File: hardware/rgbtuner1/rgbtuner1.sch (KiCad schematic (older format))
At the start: 2 parts

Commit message: some components
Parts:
- added U?: LPC811, symbol LPC811
- added U?: AL3158, symbol AL3158
- added X?: 25 MHz, symbol CRYSTAL
- D?: Description (none) -> LED 5MM RGB 640/515/461NM CLR TH; Manufacturer (none) -> Kingbright; Part Number (none) -> WP154A4SUREQBFZGC
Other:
- note added: "B G R"
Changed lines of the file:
@@
 LIBS:valves
 LIBS:rgbtuner
+LIBS:rgbtuner1-cache
 EELAYER 27 0
 EELAYER END
@@
 F 2 "~" H 4600 4100 60  0000 C CNN
 F 3 "~" H 4600 4100 60  0000 C CNN
+F 4 "Kingbright" H 4600 4100 60  0001 C CNN "Manufacturer"
+F 5 "WP154A4SUREQBFZGC" H 4600 4100 60  0001 C CNN "Part Number"
+F 6 "LED 5MM RGB 640/515/461NM CLR TH" H 4600 4100 60  0001 C CNN "Description"
 	1    4600 4100
 	0    1    1    0
@@
 Wire Wire Line
 	4450 4400 4450 4500
+$Comp
+L LPC811 U?
+U 1 1 530555B6
+P 5600 2650
+F 0 "U?" V 5550 2650 60  0000 C CNN
+F 1 "LPC811" V 5650 2650 60  0000 C CNN
+F 2 "" H 5600 2650 60  0000 C CNN
+F 3 "" H 5600 2650 60  0000 C CNN
+F 4 "NXP" H 5600 2650 60  0001 C CNN "Manufacturer"
+F 5 "LPC811M001JDH16FP" H 5600 2650 60  0001 C CNN "Part Number"
+F 6 "IC MCU ARM 8KB FLASH 16TSSOP" H 5600 2650 60  0001 C CNN "Description"
+	1    5600 2650
+	1    0    0    -1
+$EndComp
+Text Notes 4250 3800 0    60   ~ 0
+B  G  R
+$Comp
+L AL3158 U?
+U 1 1 53055893
+P 3350 2500
+F 0 "U?" H 3350 2550 60  0000 C CNN
+F 1 "AL3158" H 3350 2450 60  0000 C CNN
+F 2 "" H 3350 2500 60  0000 C CNN
+F 3 "" H 3350 2500 60  0000 C CNN
+F 4 "Diodes Inc." H 3350 2500 60  0001 C CNN "Manufacturer"
+F 5 "AL3158FSG-7" H 3350 2500 60  0001 C CNN "Part Number"
+F 6 "IC LED DRVR CHG/PMP QFN3030-20" H 3350 2500 60  0001 C CNN "Description"
+	1    3350 2500
+	1    0    0    -1
+$EndComp
+$Comp
+L CRYSTAL X?
+U 1 1 53055B71
+P 5550 1700
+F 0 "X?" H 5550 1850 60  0000 C CNN
+F 1 "25 MHz" H 5550 1550 60  0000 C CNN
+F 2 "" H 5550 1700 60  0000 C CNN
+F 3 "" H 5550 1700 60  0000 C CNN
+F 4 "Abracon" H 5550 1700 60  0001 C CNN "Manufacturer"
+F 5 "ABLS-25.000MHZ-B4-F-T" H 5550 1700 60  0001 C CNN "Part Number"
+F 6 "CRYSTAL 25MHZ 18PF SMD" H 5550 1700 60  0001 C CNN "Description"
+	1    5550 1700
+	1    0    0    -1
+$EndComp
 $EndSCHEMATC

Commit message: switched to common-anode RGB LED
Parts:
- D?: value LED-RGB-WP154 -> RGB; symbol LED-RGB-WP154 -> LED-RGB-COMMON-ANODE; Description LED 5MM RGB 640/515/461NM CLR TH -> LED - RGB Clear Common Anode; Manufacturer Kingbright -> China Young Sun LED; Note (none) -> Sparkfun COM-10820; Part Number WP154A4SUREQBFZGC -> YSL-R596AR3G4B5C-C10
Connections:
- wire segments 2 -> 1
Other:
- note removed: "B G R"
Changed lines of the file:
@@
 	1950 4350 1950 4450
 $Comp
-L LED-RGB-WP154 D?
+L LED-RGB-COMMON-ANODE D?
 U 1 1 53055340
 P 4600 4100
 F 0 "D?" H 4600 4200 50  0000 C CNN
-F 1 "LED-RGB-WP154" H 4600 3650 50  0000 C CNN
+F 1 "RGB" H 4600 3650 50  0000 C CNN
 F 2 "~" H 4600 4100 60  0000 C CNN
 F 3 "~" H 4600 4100 60  0000 C CNN
-F 4 "Kingbright" H 4600 4100 60  0001 C CNN "Manufacturer"
-F 5 "WP154A4SUREQBFZGC" H 4600 4100 60  0001 C CNN "Part Number"
-F 6 "LED 5MM RGB 640/515/461NM CLR TH" H 4600 4100 60  0001 C CNN "Description"
+F 4 "China Young Sun LED" H 4600 4100 60  0001 C CNN "Manufacturer"
+F 5 "YSL-R596AR3G4B5C-C10" H 4600 4100 60  0001 C CNN "Part Number"
+F 6 "LED - RGB Clear Common Anode" H 4600 4100 60  0001 C CNN "Description"
+F 7 "Sparkfun COM-10820" H 4600 4100 60  0001 C CNN "Note"
 	1    4600 4100
 	0    1    1    0
 $EndComp
-$Comp
-L GND #PWR?
-U 1 1 5305534F
-P 4450 4500
-F 0 "#PWR?" H 4450 4500 30  0001 C CNN
-F 1 "GND" H 4450 4430 30  0001 C CNN
-F 2 "" H 4450 4500 60  0000 C CNN
-F 3 "" H 4450 4500 60  0000 C CNN
-	1    4450 4500
-	1    0    0    -1
-$EndComp
-Wire Wire Line
-	4450 4400 4450 4500
 $Comp
 L LPC811 U?
@@
 	1    0    0    -1
 $EndComp
-Text Notes 4250 3800 0    60   ~ 0
-B  G  R
 $Comp
 L AL3158 U?

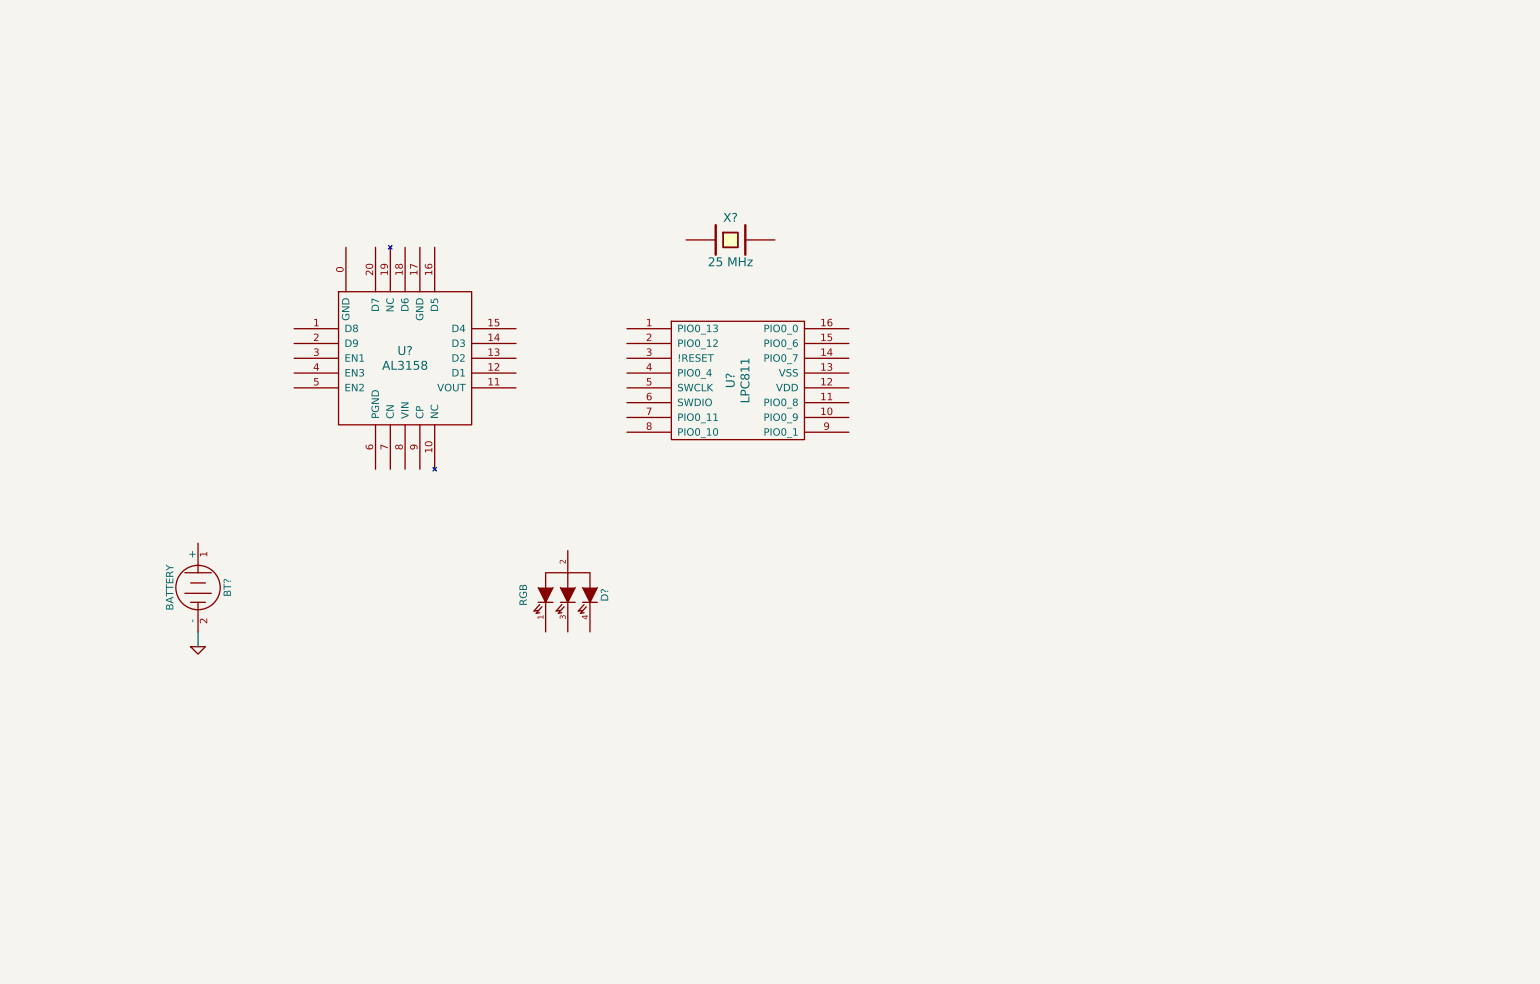
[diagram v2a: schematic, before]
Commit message: LED driver connections
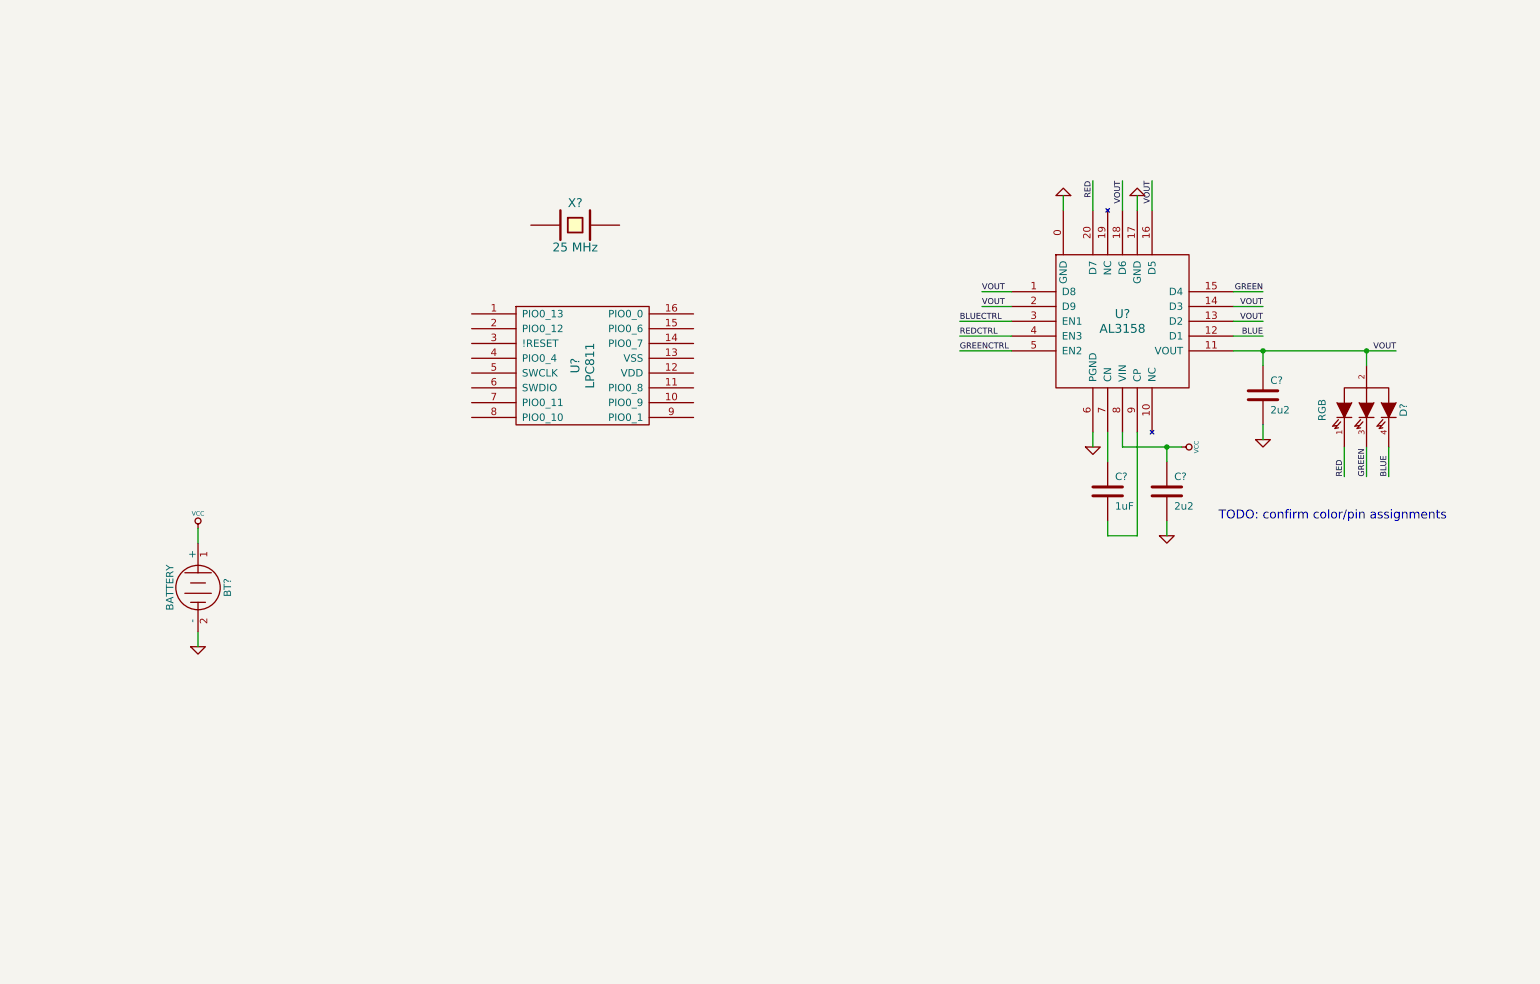
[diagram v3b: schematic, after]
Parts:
- added C? (x2): 2u2, symbol C
- added C?: 1uF, symbol C
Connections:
- net GND: now also U?.0 (GND), U?.17 (GND), U?.6 (PGND), C?.2, C?.2
- net VCC: now reaches BT?.1 (+)
- net VCC: now also U?.8 (VIN), C?.1
- net RED: now reaches D?.1 (RED)
- net RED: now also U?.20 (D7)
- net VOUT: now reaches D?.2 (A)
- net VOUT: now also U?.1 (D8), U?.11 (VOUT), U?.13 (D2), U?.14 (D3), U?.16 (D5), U?.18 (D6), U?.2 (D9), C?.1
- net GREEN: now reaches D?.3 (GREEN)
- net GREEN: now also U?.15 (D4)
- net BLUE: now reaches D?.4 (BLUE)
- net BLUE: now also U?.12 (D1)
- net BLUECTRL: now reaches U?.3 (EN1)
- net REDCTRL: now reaches U?.4 (EN3)
- net GREENCTRL: now reaches U?.5 (EN2)
- net at U?.7 (CN): now also C?.1
- net at U?.9 (CP): now also C?.2
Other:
- note added: "TODO: confirm color/pin assignments"
- moved on the sheet: D?, U?, X?

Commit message: MCU
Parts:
- added C? (x3): C, symbol C
- added P?: CONN_2, symbol CONN_2
- added R? (x7): 10k, symbol R
- U?: symbol LPC811 -> LPC812-20
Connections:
- net BLUECTRL: now also U?.2 (PIO0_13), R?.2
- net GND: now also U?.15 (VDD), C?.2, C?.2, C?.2, R?.1, R?.1, R?.1
- net GREENCTRL: now also U?.20 (PIO0_14), R?.2
- net REDCTRL: now also U?.1 (PIO0_17), R?.2
- net VCC: now also U?.16 (VSS), C?.1, P?.2 (PM), R?.1, R?.2, R?.2, R?.2; no longer BT?.1 (+)
- net S5: now reaches U?.10 (PIO0_16)
- net S2: now reaches U?.11 (PIO0_15)
- net LED1: now reaches U?.12 (PIO0_1)
- net LED1: now also R?.2
- net at U?.13 (PIO0_9): now also X?.2, C?.1
- net at U?.14 (PIO0_8): now also X?.1, C?.1
- net COMA: now reaches U?.3 (PIO0_12)
- net COMA: now also R?.1
- net RESET: now reaches U?.4 (!RESET)
- net RESET: now also R?.1
- net COMB: now reaches U?.5 (PIO0_4)
- net COMB: now also R?.1
- net SWCLK: now reaches U?.6 (SWCLK)
- net SWDIO: now reaches U?.7 (SWDIO)
- net S3: now reaches U?.8 (PIO0_11)
- net S4: now reaches U?.9 (PIO0_10)
- new net: BT?.1 (+), P?.1 (P1)
- new net LED2: U?.19 (PIO0_0)
- new net LED3: U?.18 (PIO0_6)
- new net LED4: U?.17 (PIO0_7)
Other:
- note added: "FIXME: WAKEUP"
- note added: "PCB jumper"
- note added: "TODO:\nSWD\nISP?\ndirectional input\ncharlieplexed indicator LEDs"
- moved on the sheet: X?

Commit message: charlieplexed indicator LEDs, WAKEUP fix
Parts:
- added D? (x10): LED, symbol LED
- added R? (x4): 10k, symbol R
- added R? (x4): R, symbol R
- C? (x2): value C -> 33pF
- R? (x2): value 10k -> 100k
- R?: Note (none) -> DNP
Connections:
- net COMA: now also R?.1, U?.5 (PIO0_4); no longer R?.1, U?.3 (PIO0_12)
- net COMB: now also R?.1, U?.3 (PIO0_12); no longer R?.1, U?.5 (PIO0_4)
- net GND: now also R?.1, R?.1, R?.1, R?.1
- net LED1: now also R?.1
- net LED2: now also R?.1
- net LED3: now also R?.1
- net LED4: now also R?.1
- net S2: now also R?.2
- net S3: now also R?.2
- net S4: now also R?.2
- net S5: now also R?.2
- new net: D?.1 (A), D?.1 (A), D?.2 (K), D?.2 (K), R?.2 (x2)
- new net: D?.1 (A), D?.1 (A), D?.1 (A), D?.2 (K), D?.2 (K), D?.2 (K), R?.2 (x2)
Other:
- note added: "TODO:\nSWD\nISP?\ndirectional input"
- note removed: "FIXME: WAKEUP"
- note removed: "TODO:\nSWD\nISP?\ndirectional input\ncharlieplexed indicator LEDs"

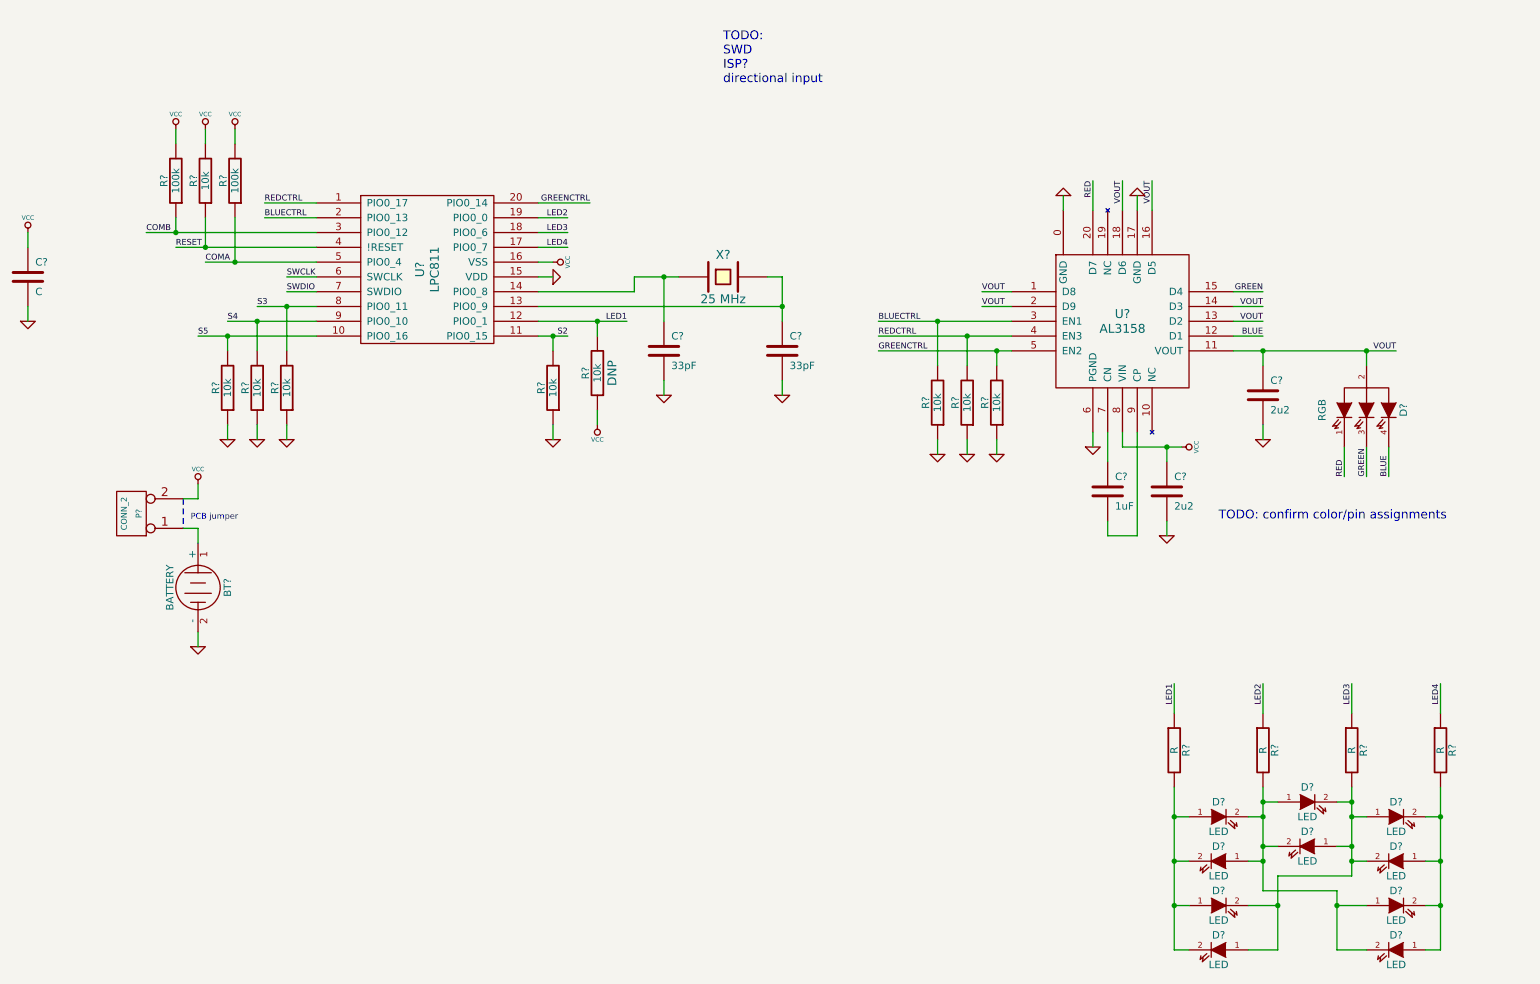
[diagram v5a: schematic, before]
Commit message: directional input
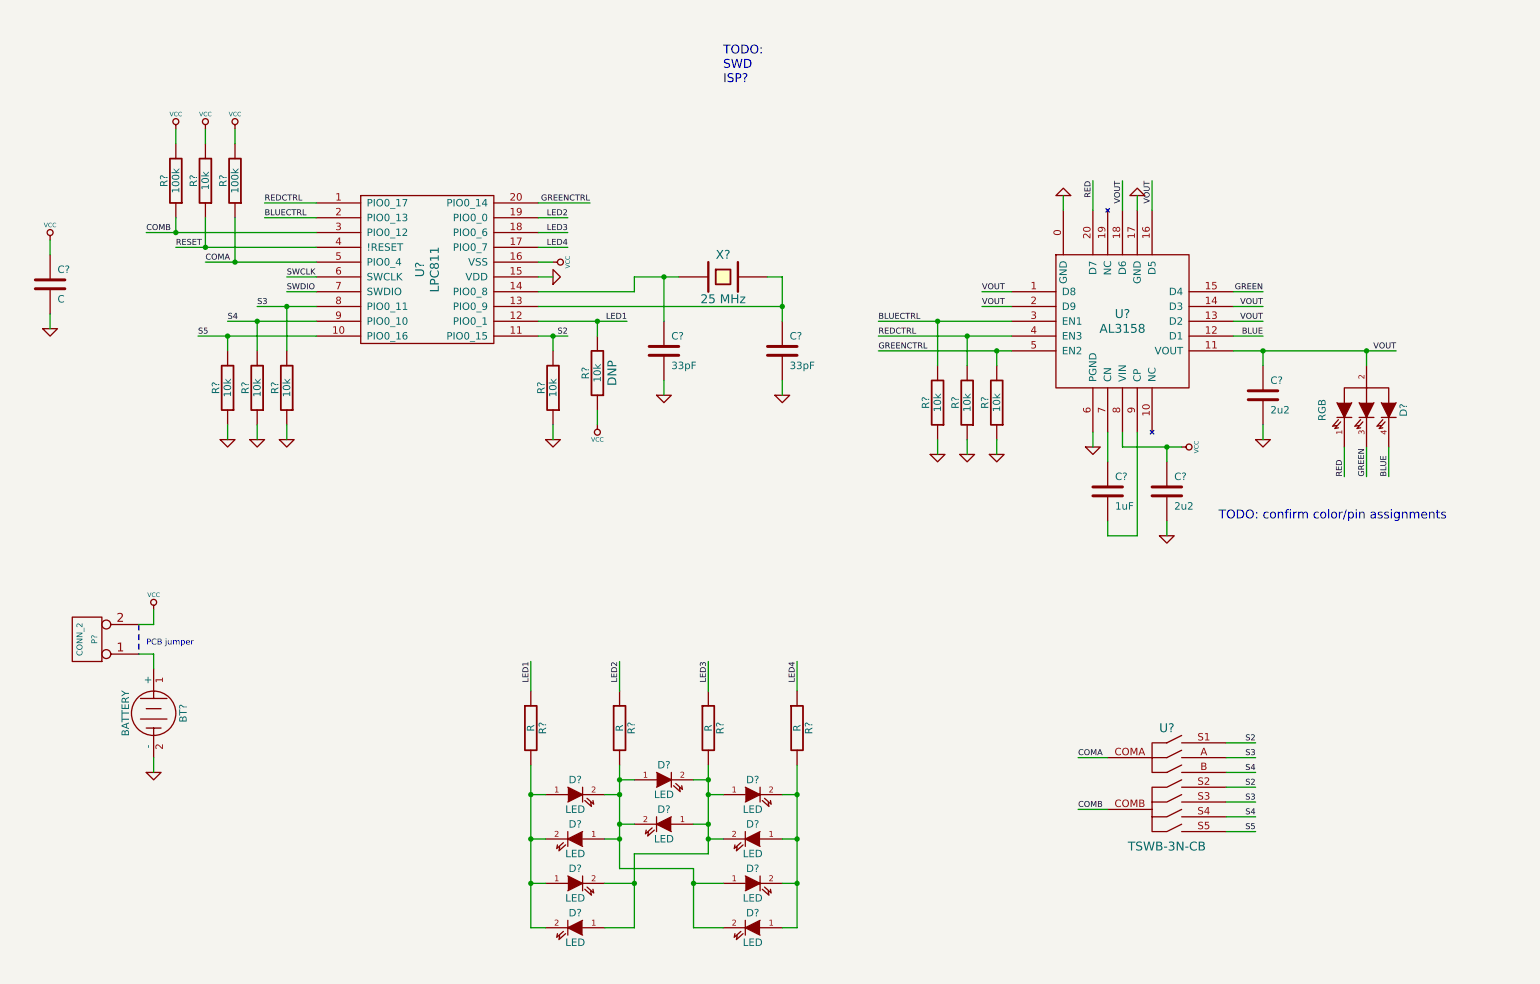
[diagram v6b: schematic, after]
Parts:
- added U?: TSWB-3N-CB, symbol TSWB-3N-CB
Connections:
- net COMA: now also U?.COMA
- net COMB: now also U?.COMB
- net S2: now also U?.S1, U?.S2
- net S3: now also U?.A, U?.S3
- net S4: now also U?.B, U?.S4
- net S5: now also U?.S5
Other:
- note added: "TODO:\nSWD\nISP?"
- note removed: "TODO:\nSWD\nISP?\ndirectional input"
- moved on the sheet: BT?, C?, D?, P?, R?
